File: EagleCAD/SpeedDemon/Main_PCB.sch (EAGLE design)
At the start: 76 parts, among them Q1 DMC2700, Q2 BSS138L, U2 NC7S08M, U3 LM3676, U4 STM32F072-LQFP48, X1 32.768kHz

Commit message: final layout adjustments
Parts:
- added R33: 10k, rcl:R-US_R0805
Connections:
- net FL_SWCLK: now also R33.2
- net GND: now also R33.1
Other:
- note added: "Either pull-up or pull-dwn resistor on SWCLK is DNP"
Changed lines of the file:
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@@
 <part name="C24" library="0805_generics" deviceset="C_0805_NP" device="" value="100nF"/>
 <part name="D4" library="LCRD_SMD_generics" deviceset="1N4148_SOD_123" device="" value="1N4148"/>
+<part name="R33" library="rcl" library_urn="urn:adsk.eagle:library:334" deviceset="R-US_" device="R0805" package3d_urn="urn:adsk.eagle:package:23553/2" value="10k"/>
+<part name="GND27" library="supply1" library_urn="urn:adsk.eagle:library:371" deviceset="GND" device=""/>
 </parts>
 <sheets>
@@
 <text x="37" y="59.5" size="0.4064" layer="97">Debounce circuitry. Can bypass
 if voltages out of range for AND gate.</text>
+<text x="320.04" y="190.5" size="1.778" layer="97">Either pull-up or pull-dwn resistor on SWCLK is DNP</text>
 </plain>
 <instances>
@@
 <attribute name="VALUE" x="57.1246" y="76.7842" size="1.778" layer="96"/>
 </instance>
+<instance part="R33" gate="G$1" x="312.42" y="193.04" rot="R90"/>
+<instance part="GND27" gate="1" x="312.42" y="182.88"/>
 </instances>
 <busses>
@@
 <segment>
 <pinref part="U4" gate="G$1" pin="PA14/USART2_TX/SWCLK"/>
-<wire x1="365.76" y1="198.12" x2="281.94" y2="198.12" width="0.1524" layer="91"/>
+<wire x1="365.76" y1="198.12" x2="312.42" y2="198.12" width="0.1524" layer="91"/>
 <pinref part="R9" gate="G$1" pin="1"/>
+<wire x1="312.42" y1="198.12" x2="281.94" y2="198.12" width="0.1524" layer="91"/>
 <wire x1="281.94" y1="198.12" x2="281.94" y2="144.78" width="0.1524" layer="91"/>
 <wire x1="281.94" y1="144.78" x2="256.54" y2="144.78" width="0.1524" layer="91"/>
@@
 <label x="257.048" y="145.288" size="0.8128" layer="95"/>
 <label x="287.02" y="198.755" size="1.6764" layer="95"/>
+<pinref part="R33" gate="G$1" pin="2"/>
+<junction x="312.42" y="198.12"/>
 </segment>
 </net>
@@
 <junction x="154.94" y="109.22"/>
 </segment>
-</net>
+<segment>
+<pinref part="R33" gate="G$1" pin="1"/>
+<pinref part="GND27" gate="1" pin="GND"/>
+<wire x1="312.42" y1="185.42" x2="312.42" y2="187.96" width="0.1524" layer="91"/>
+</segment>
+</net>

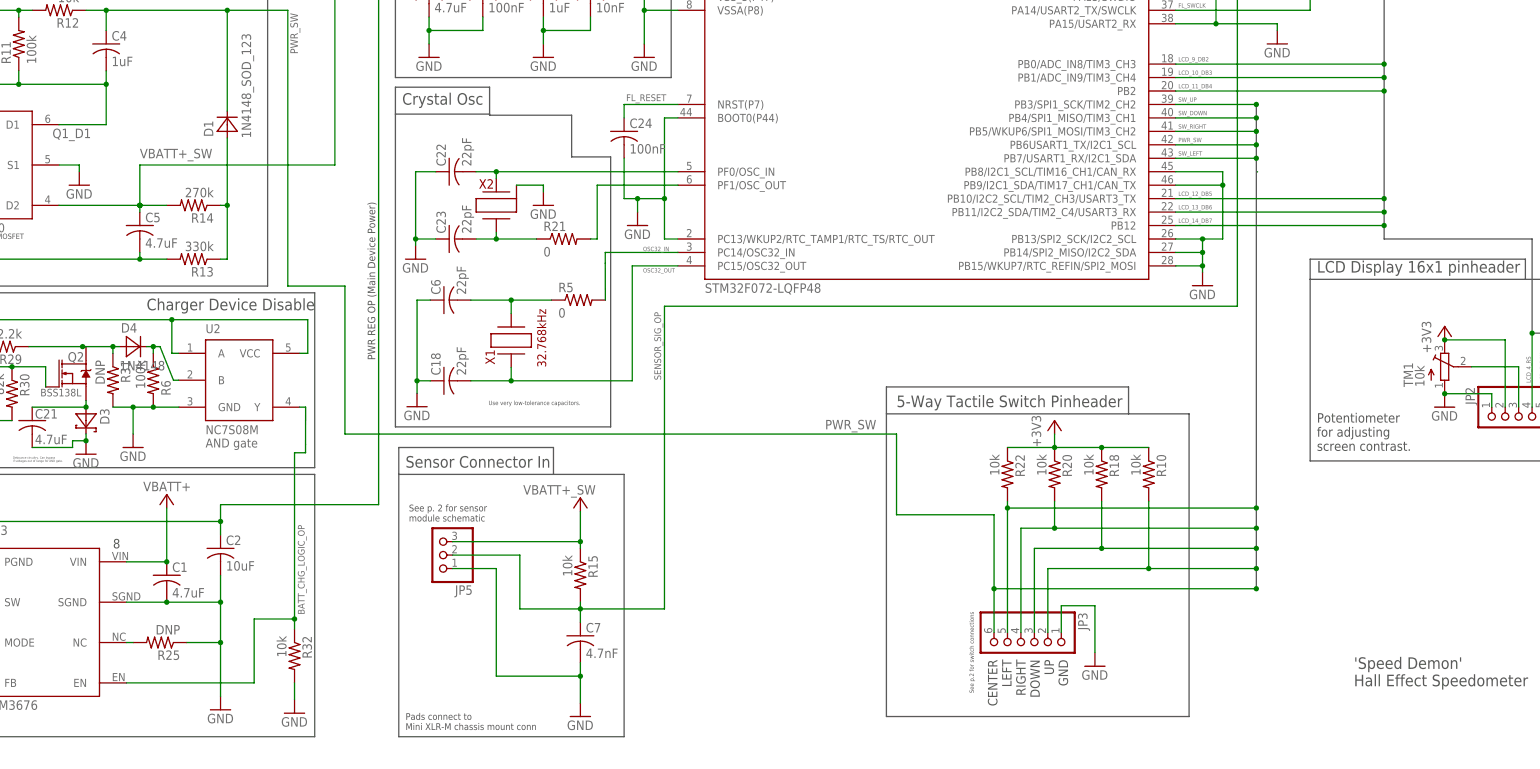
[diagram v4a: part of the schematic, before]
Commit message: Final Board/schem. Includes added debounce circuit for 5-way switch.
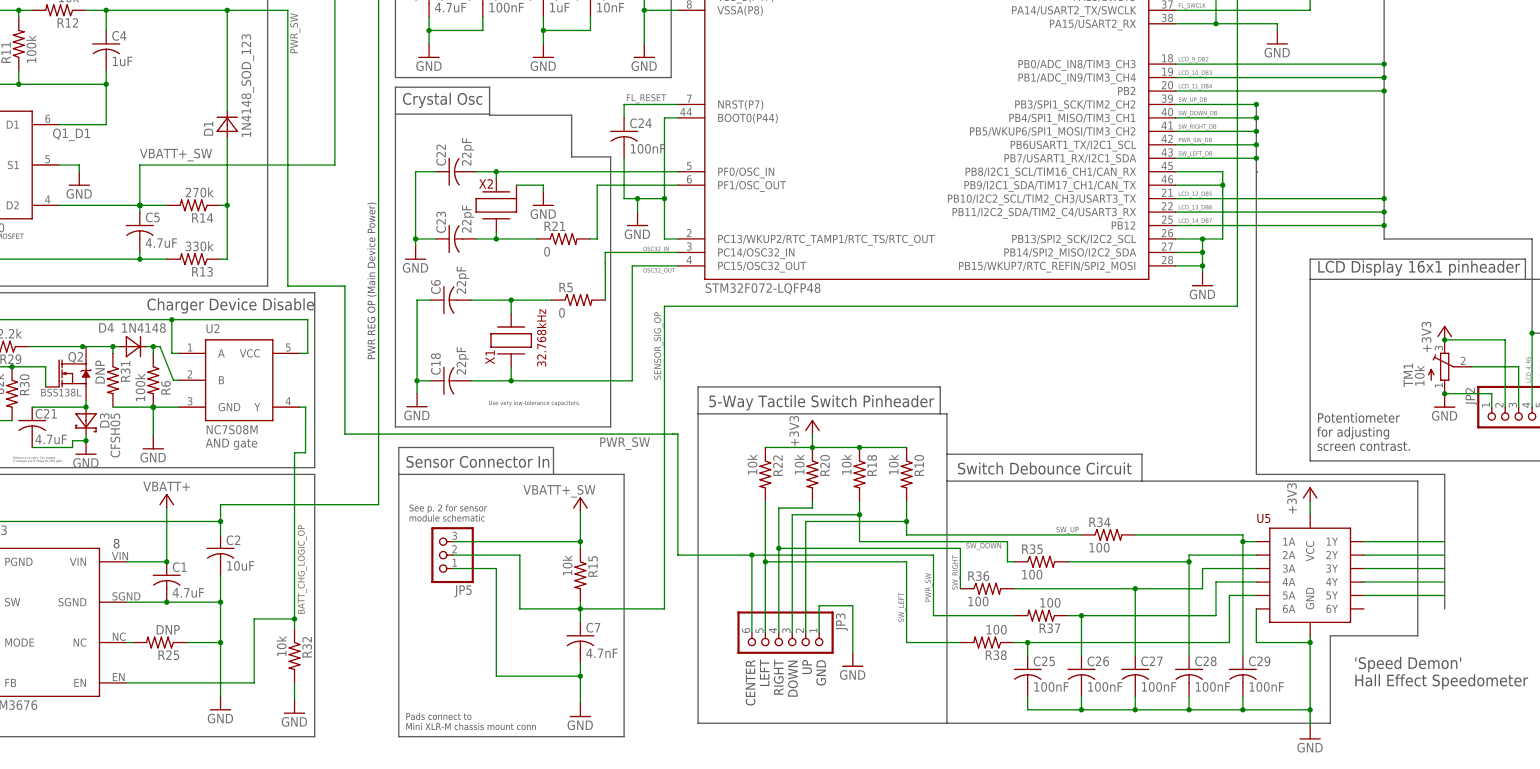
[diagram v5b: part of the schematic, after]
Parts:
- added C25, C26, C27, C28, C29: 100nF, 0805_generics:C_0805_NP
- added R34, R35, R36, R37, R38: 100, 0805_generics:R_0805
- added U5: (no value), DMC2700:SN74LV14A_HEX_SHMITT
- D3: value (none) -> CFSH05
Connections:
- new net N$21: C25.1, R38.1, U5.5A
- new net N$22: C26.1, R37.1, U5.4A
- new net N$23: C27.1, R36.2, U5.3A
- new net N$24: C28.1, R35.2, U5.2A
- new net N$26: C29.1, R34.2, U5.1A
- new net PWR_SW_DB: U4.PB6USART1_TX/I2C1_SCL, U5.4Y
- new net SW_DOWN_DB: U4.PB4/SPI1_MISO/TIM3_CH1, U5.2Y
- new net SW_LEFT_DB: U4.PB7/USART1_RX/I2C1_SDA, U5.5Y
- new net SW_RIGHT_DB: U4.PB5/WKUP6/SPI1_MOSI/TIM3_CH2, U5.3Y
- new net SW_UP_DB: U4.PB3/SPI1_SCK/TIM2_CH2, U5.1Y
- net +3V3: now also U5.VCC
- net GND: now also C25.2, C26.2, C27.2, C28.2, C29.2, U5.6A, U5.GND
- net PWR_SW: now also R37.2; no longer U4.PB6USART1_TX/I2C1_SCL
- net SW_DOWN: now also R35.1; no longer U4.PB4/SPI1_MISO/TIM3_CH1
- net SW_LEFT: now also R38.2; no longer U4.PB7/USART1_RX/I2C1_SDA
- net SW_RIGHT: now also R36.1; no longer U4.PB5/WKUP6/SPI1_MOSI/TIM3_CH2
- net SW_UP: now also R34.1; no longer U4.PB3/SPI1_SCK/TIM2_CH2
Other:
- note added: "Switch Debounce Circuit"
- note removed: "See p.2 for switch connections"
- moved on the sheet: JP3, R10, R18, R20, R22
